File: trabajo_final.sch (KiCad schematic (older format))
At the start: 0 parts

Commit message: cambio de pc
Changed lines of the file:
@@
 F8 "SDA" B R 2750 2050 60
 F9 "SCL" B R 2750 2150 60
-F10 "RXD" B R 2750 2350 60
-F11 "TXD" B R 2750 2450 60
+F10 "RXD" I R 2750 2350 60
+F11 "TXD" O R 2750 2450 60
 F12 "RD" B R 2750 2650 60
 F13 "TD" B R 2750 2750 60
@@
 F23 "LCD_EN" I R 2750 5500 60
 F24 "GPIO0" B R 2750 5750 60
-F25 "GPIO2" B R 2750 5950 60
-F26 "GPIO4" B R 2750 6150 60
-F27 "GPIO6" B R 2750 6350 60
+F25 "GPIO2" I R 2750 5950 60
+F26 "GPIO4" O R 2750 6150 60
+F27 "GPIO6" O R 2750 6350 60
 F28 "RXD1" B R 2750 4250 60
 F29 "TXEN" B R 2750 4050 60
@@
 F40 "LCD2" B R 2750 5200 60
 F41 "LCD1" B R 2750 5100 60
-F42 "GPIO1" B R 2750 5850 60
-F43 "GPIO3" B R 2750 6050 60
-F44 "GPIO5" B R 2750 6250 60
+F42 "GPIO1" O R 2750 5850 60
+F43 "GPIO3" O R 2750 6050 60
+F44 "GPIO5" O R 2750 6250 60
 F45 "GPIO7" B R 2750 6450 60
 F46 "GPIO8" B R 2750 6550 60
@@
 Text Notes 3800 2000 0    60   Italic 12
 I2C
-Text Notes 3750 2300 0    60   Italic 12
+Text Notes 3700 2300 0    60   Italic 12
 RS-232
-Text Notes 3300 5700 0    60   Italic 12
+Text Notes 3300 5800 0    60   Italic 12
 E/S PROPÓSITOS GENERALES
 Wire Wire Line
@@
 F2 "SDA" B L 5250 2050 60
 F3 "SCL" I L 5250 2150 60
-F4 "GPIO6" B L 5250 6350 60
+F4 "GPIO6" I L 5250 6350 60
 F5 "RS232_RXD" O L 5250 2350 60
 F6 "RS232_TXD" I L 5250 2450 60

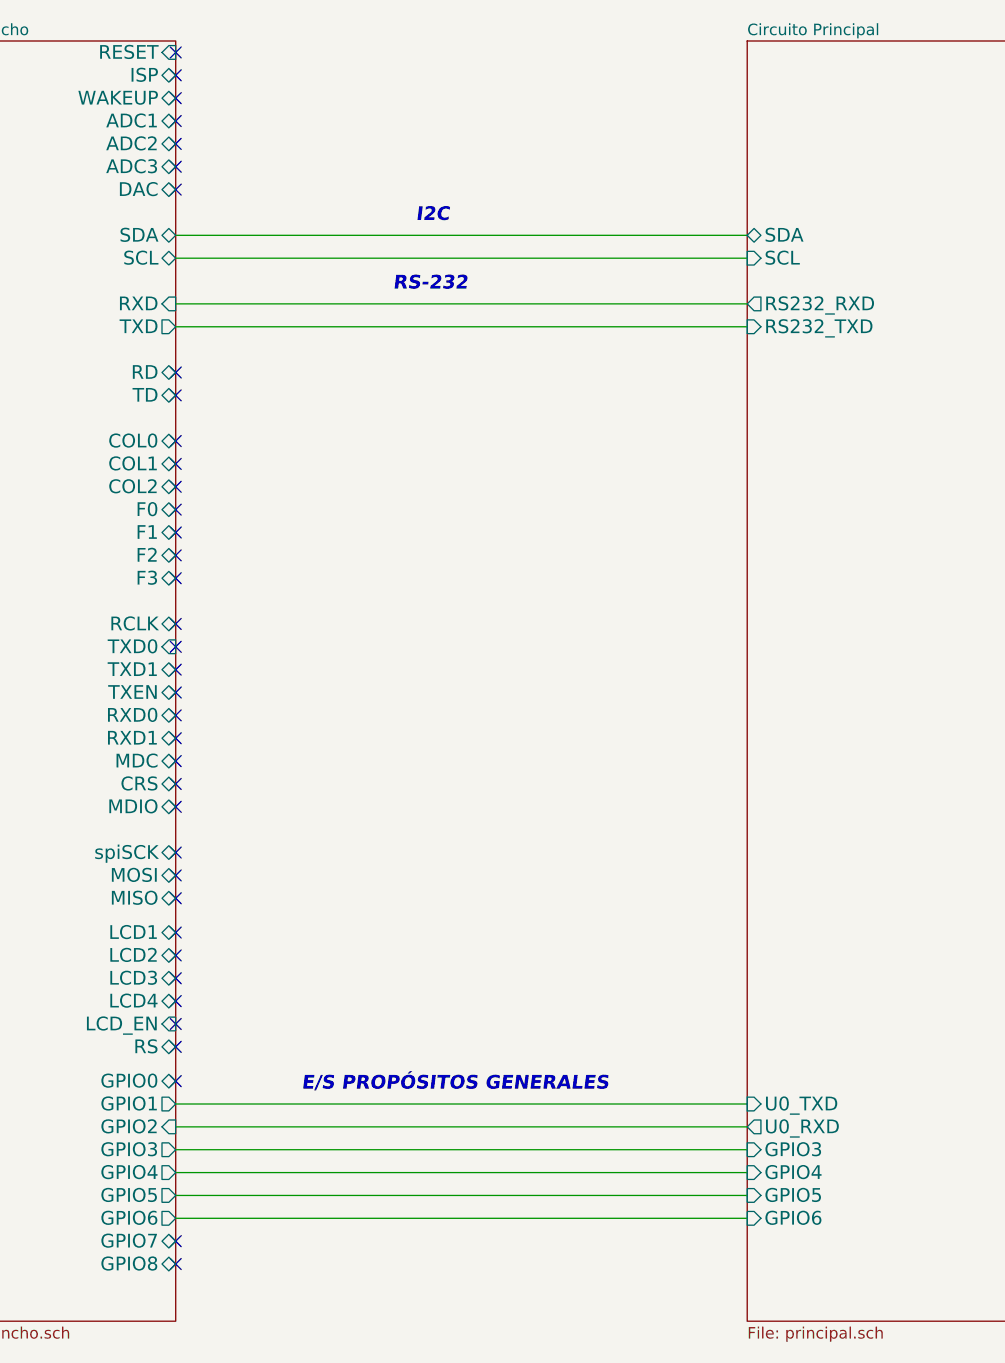
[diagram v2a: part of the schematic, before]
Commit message: agregado buzzer y medidor de batería
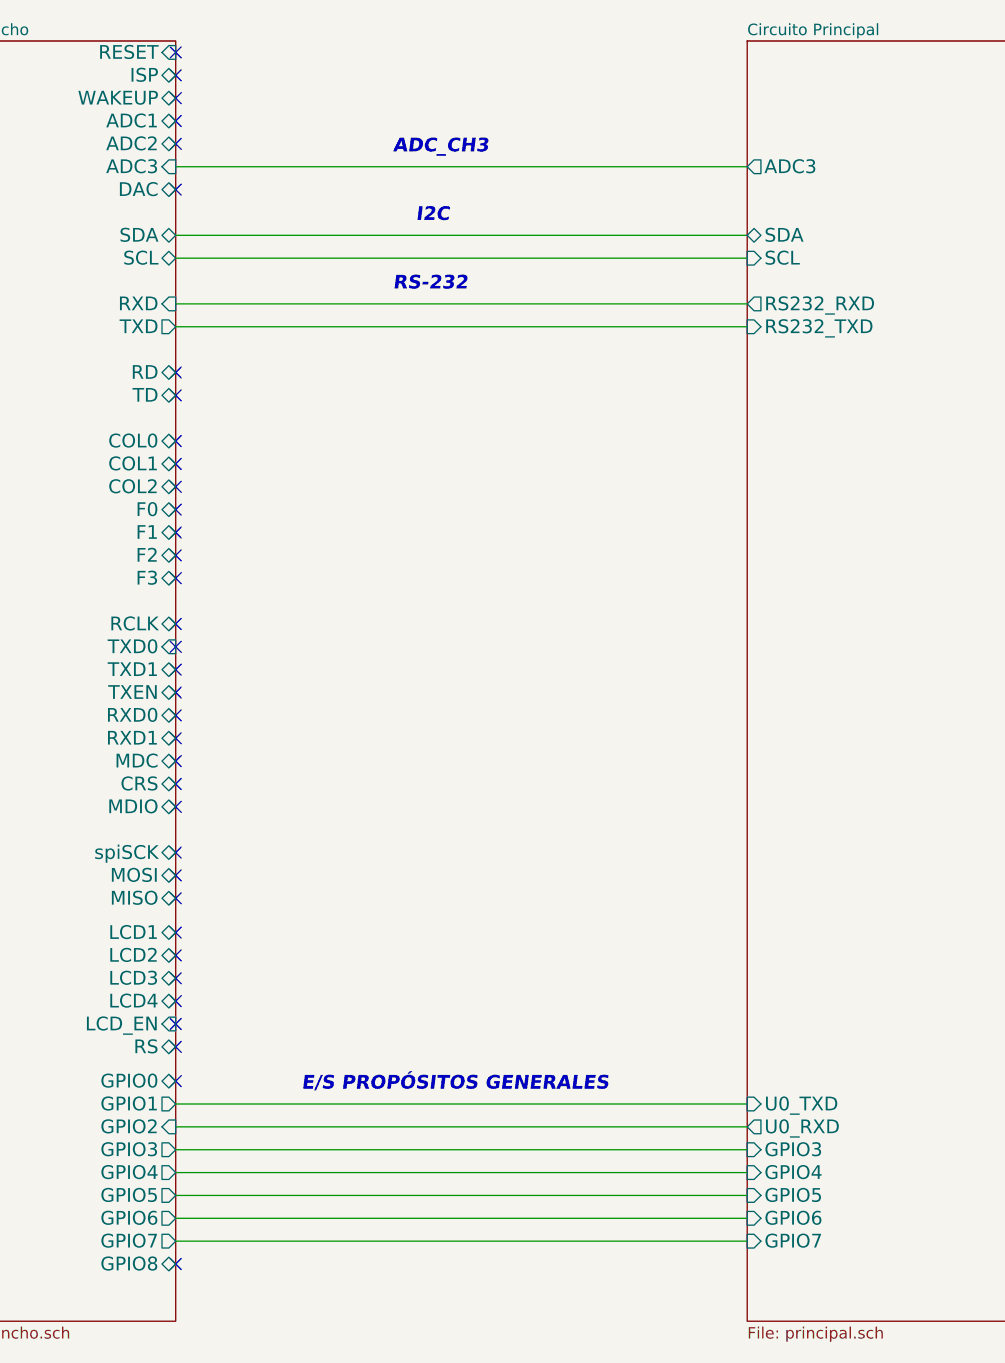
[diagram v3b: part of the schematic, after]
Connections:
- no-connect marks 37 -> 35
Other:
- note added: "ADC_CH3"
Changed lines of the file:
@@
 LIBS:falling_detector-cache
 LIBS:poncho_grande-cache
+LIBS:74xgxx
+LIBS:74xx
+LIBS:ac-dc
+LIBS:actel
+LIBS:adc-dac
+LIBS:Altera
+LIBS:analog_devices
+LIBS:analog_switches
+LIBS:atmel
+LIBS:audio
+LIBS:brooktre
+LIBS:cmos_ieee
+LIBS:cmos4000
+LIBS:conn
+LIBS:contrib
+LIBS:cypress
+LIBS:dc-dc
+LIBS:device
+LIBS:digital-audio
+LIBS:diode
+LIBS:display
+LIBS:dsp
+LIBS:elec-unifil
+LIBS:ESD_Protection
+LIBS:ftdi
+LIBS:gennum
+LIBS:graphic
+LIBS:hc11
+LIBS:intel
+LIBS:interface
+LIBS:ir
+LIBS:Lattice
+LIBS:linear
+LIBS:logo
+LIBS:maxim
+LIBS:memory
+LIBS:microchip
+LIBS:microchip_dspic33dsc
+LIBS:microchip_pic10mcu
+LIBS:microchip_pic12mcu
+LIBS:microchip_pic16mcu
+LIBS:microchip_pic18mcu
+LIBS:microchip_pic32mcu
+LIBS:microcontrollers
+LIBS:motor_drivers
+LIBS:motorola
+LIBS:msp430
+LIBS:nordicsemi
+LIBS:nxp_armmcu
+LIBS:onsemi
+LIBS:opto
+LIBS:Oscillators
+LIBS:philips
+LIBS:power
+LIBS:Power_Management
+LIBS:powerint
+LIBS:pspice
+LIBS:references
+LIBS:regul
+LIBS:relays
+LIBS:rfcom
+LIBS:sensors
+LIBS:silabs
+LIBS:siliconi
+LIBS:stm8
+LIBS:stm32
+LIBS:supertex
+LIBS:switches
+LIBS:texas
+LIBS:transf
+LIBS:transistors
+LIBS:ttl_ieee
+LIBS:valves
+LIBS:video
+LIBS:Xicor
+LIBS:xilinx
+LIBS:Zilog
+LIBS:buzzer
 LIBS:trabajo_final-cache
 EELAYER 25 0
@@
 F2 "RESET" I R 2750 1250 60
 F3 "ISP" B R 2750 1350 60
-F4 "ADC3" B R 2750 1750 60
+F4 "ADC3" I R 2750 1750 60
 F5 "ADC2" B R 2750 1650 60
 F6 "ADC1" B R 2750 1550 60
@@
 F43 "GPIO3" O R 2750 6050 60
 F44 "GPIO5" O R 2750 6250 60
-F45 "GPIO7" B R 2750 6450 60
+F45 "GPIO7" O R 2750 6450 60
 F46 "GPIO8" B R 2750 6550 60
 F47 "COL2" B R 2750 3150 60
@@
 Text Notes 3300 5800 0    60   Italic 12
 E/S PROPÓSITOS GENERALES
-Wire Wire Line
-	5250 6350 2750 6350
-Wire Wire Line
-	2750 6250 5250 6250
-Wire Wire Line
-	5250 6150 2750 6150
-Wire Wire Line
-	2750 6050 5250 6050
-Wire Wire Line
-	5250 5950 2750 5950
-Wire Wire Line
-	5250 5850 2750 5850
-Wire Wire Line
-	5250 2450 2750 2450
-Wire Wire Line
-	2750 2350 5250 2350
-Wire Wire Line
-	2750 2150 5250 2150
-Wire Wire Line
-	5250 2050 2750 2050
 $Comp
 L Logo_Poncho #G1
@@
 F10 "U0_TXD" I L 5250 5850 60
 F11 "U0_RXD" O L 5250 5950 60
+F12 "ADC3" O L 5250 1750 60
+F13 "GPIO7" I L 5250 6450 60
 $EndSheet
 NoConn ~ 2750 1250
@@
 NoConn ~ 2750 1550
 NoConn ~ 2750 1650
-NoConn ~ 2750 1750
 NoConn ~ 2750 1850
 NoConn ~ 2750 2650
@@
 NoConn ~ 2750 5750
 NoConn ~ 2750 6550
-NoConn ~ 2750 6450
+Text Notes 3700 1700 0    60   Italic 12
+ADC_CH3
+Wire Wire Line
+	5250 6450 2750 6450
+Wire Wire Line
+	5250 1750 2750 1750
+Wire Wire Line
+	5250 2050 2750 2050
+Wire Wire Line
+	2750 2150 5250 2150
+Wire Wire Line
+	2750 2350 5250 2350
+Wire Wire Line
+	5250 2450 2750 2450
+Wire Wire Line
+	5250 5850 2750 5850
+Wire Wire Line
+	5250 5950 2750 5950
+Wire Wire Line
+	2750 6050 5250 6050
+Wire Wire Line
+	5250 6150 2750 6150
+Wire Wire Line
+	2750 6250 5250 6250
+Wire Wire Line
+	5250 6350 2750 6350
 $EndSCHEMATC

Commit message: ruteo casi terminado
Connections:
- no-connect marks 35 -> 36
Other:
- note added: "UART0"
- note added: "UART3"
- note removed: "RS-232"
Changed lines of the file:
@@
 encoding utf-8
 Sheet 1 3
-Title "Poncho"
-Date "2016-05-17"
-Rev "1.0"
-Comp "GMotion"
-Comment1 "Autor: Matías Dell'Oso"
-Comment2 ""
+Title "Connections"
+Date "2016-07-23"
+Rev "2.0"
+Comp "Proyecto CIAA - COMPUTADORA INDUSTRIAL ABIERTA ARGENTINA"
+Comment1 "https://github.com/mdelloso/falling_detector"
+Comment2 "Autores y Licencia del template (Matías Dell'Oso - UNLP)"
 Comment3 ""
 Comment4 ""
@@
 F22 "MOSI" B R 2750 4850 60
 F23 "LCD_EN" I R 2750 5500 60
-F24 "GPIO0" B R 2750 5750 60
+F24 "GPIO0" B R 2750 6150 60
 F25 "GPIO2" I R 2750 5950 60
-F26 "GPIO4" O R 2750 6150 60
-F27 "GPIO6" O R 2750 6350 60
+F26 "GPIO4" O R 2750 6350 60
+F27 "GPIO6" O R 2750 6550 60
 F28 "RXD1" B R 2750 4250 60
 F29 "TXEN" B R 2750 4050 60
@@
 F41 "LCD1" B R 2750 5100 60
 F42 "GPIO1" O R 2750 5850 60
-F43 "GPIO3" O R 2750 6050 60
-F44 "GPIO5" O R 2750 6250 60
-F45 "GPIO7" O R 2750 6450 60
-F46 "GPIO8" B R 2750 6550 60
+F43 "GPIO3" O R 2750 6250 60
+F44 "GPIO5" O R 2750 6450 60
+F45 "GPIO7" O R 2750 6650 60
+F46 "GPIO8" B R 2750 6750 60
 F47 "COL2" B R 2750 3150 60
 F48 "WAKEUP" B R 2750 1450 60
 $EndSheet
-Text Notes 3800 2000 0    60   Italic 12
+Text Notes 3900 2000 0    60   Italic 12
 I2C
-Text Notes 3700 2300 0    60   Italic 12
-RS-232
-Text Notes 3300 5800 0    60   Italic 12
+Text Notes 3850 2300 0    60   Italic 12
+UART3
+Text Notes 3300 6200 0    60   Italic 12
 E/S PROPÓSITOS GENERALES
 $Comp
@@
 F2 "SDA" B L 5250 2050 60
 F3 "SCL" I L 5250 2150 60
-F4 "GPIO6" I L 5250 6350 60
+F4 "GPIO6" I L 5250 6550 60
 F5 "RS232_RXD" O L 5250 2350 60
 F6 "RS232_TXD" I L 5250 2450 60
-F7 "GPIO3" I L 5250 6050 60
-F8 "GPIO4" I L 5250 6150 60
-F9 "GPIO5" I L 5250 6250 60
+F7 "GPIO3" I L 5250 6250 60
+F8 "GPIO4" I L 5250 6350 60
+F9 "GPIO5" I L 5250 6450 60
 F10 "U0_TXD" I L 5250 5850 60
 F11 "U0_RXD" O L 5250 5950 60
 F12 "ADC3" O L 5250 1750 60
-F13 "GPIO7" I L 5250 6450 60
+F13 "GPIO7" I L 5250 6650 60
 $EndSheet
 NoConn ~ 2750 1250
@@
 NoConn ~ 2750 5600
 NoConn ~ 2750 5750
-NoConn ~ 2750 6550
-Text Notes 3700 1700 0    60   Italic 12
+NoConn ~ 2750 6750
+Text Notes 3800 1700 0    60   Italic 12
 ADC_CH3
 Wire Wire Line
@@
 	5250 5950 2750 5950
 Wire Wire Line
-	2750 6050 5250 6050
-Wire Wire Line
-	5250 6150 2750 6150
-Wire Wire Line
 	2750 6250 5250 6250
 Wire Wire Line
 	5250 6350 2750 6350
+Wire Wire Line
+	5250 6650 2750 6650
+Wire Wire Line
+	5250 6550 2750 6550
+NoConn ~ 2750 6150
+Text Notes 3800 5800 0    60   Italic 12
+UART0
 $EndSCHEMATC

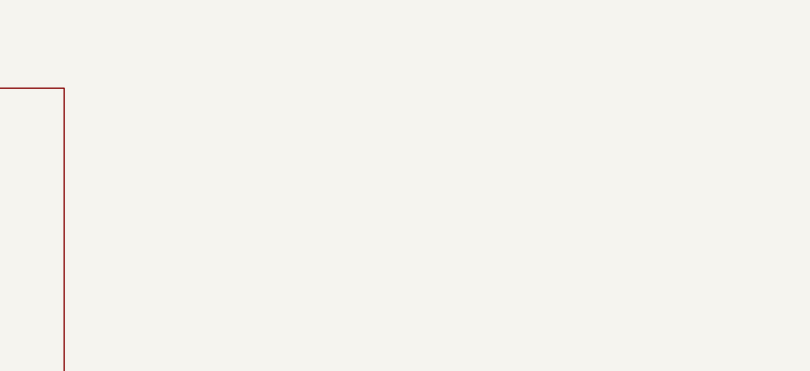
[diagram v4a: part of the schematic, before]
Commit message: Realizando las correcciones correspondientes a la Revision 1
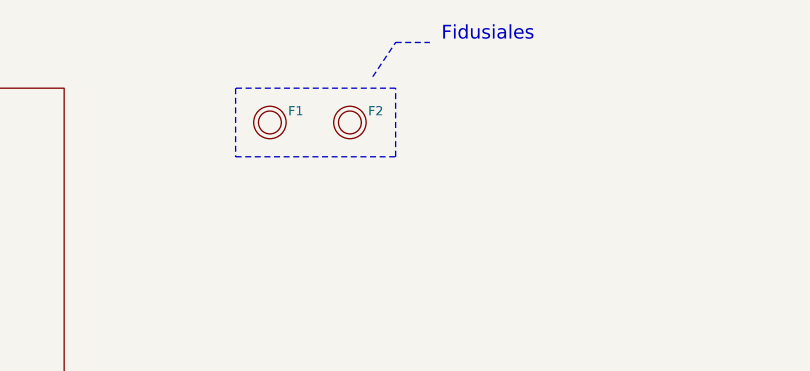
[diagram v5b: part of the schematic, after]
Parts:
- added F1, F2: FIDUCIAL, footprints:Fiducial_1mm, symbol FIDUCIAL
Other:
- note added: "Fidusiales"
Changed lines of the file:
@@
 LIBS:falling_detector-cache
 LIBS:poncho_grande-cache
-LIBS:74xgxx
-LIBS:74xx
-LIBS:ac-dc
-LIBS:actel
-LIBS:adc-dac
-LIBS:Altera
-LIBS:analog_devices
-LIBS:analog_switches
-LIBS:atmel
-LIBS:audio
-LIBS:brooktre
-LIBS:cmos_ieee
-LIBS:cmos4000
-LIBS:conn
-LIBS:contrib
-LIBS:cypress
-LIBS:dc-dc
-LIBS:device
-LIBS:digital-audio
-LIBS:diode
-LIBS:display
-LIBS:dsp
-LIBS:elec-unifil
-LIBS:ESD_Protection
-LIBS:ftdi
-LIBS:gennum
-LIBS:graphic
-LIBS:hc11
-LIBS:intel
-LIBS:interface
-LIBS:ir
-LIBS:Lattice
-LIBS:linear
-LIBS:logo
-LIBS:maxim
-LIBS:memory
-LIBS:microchip
-LIBS:microchip_dspic33dsc
-LIBS:microchip_pic10mcu
-LIBS:microchip_pic12mcu
-LIBS:microchip_pic16mcu
-LIBS:microchip_pic18mcu
-LIBS:microchip_pic32mcu
-LIBS:microcontrollers
-LIBS:motor_drivers
-LIBS:motorola
-LIBS:msp430
-LIBS:nordicsemi
-LIBS:nxp_armmcu
-LIBS:onsemi
-LIBS:opto
-LIBS:Oscillators
-LIBS:philips
+LIBS:buzzer
 LIBS:power
-LIBS:Power_Management
-LIBS:powerint
-LIBS:pspice
-LIBS:references
-LIBS:regul
-LIBS:relays
-LIBS:rfcom
-LIBS:sensors
-LIBS:silabs
-LIBS:siliconi
-LIBS:stm8
-LIBS:stm32
-LIBS:supertex
-LIBS:switches
-LIBS:texas
-LIBS:transf
-LIBS:transistors
-LIBS:ttl_ieee
-LIBS:valves
-LIBS:video
-LIBS:Xicor
-LIBS:xilinx
-LIBS:Zilog
-LIBS:buzzer
+LIBS:ej2cese
 LIBS:trabajo_final-cache
 EELAYER 25 0
@@
 Text Notes 3800 5800 0    60   Italic 12
 UART0
+$Comp
+L FIDUCIAL F1
+U 1 1 579982BE
+P 7500 1350
+F 0 "F1" H 7580 1400 40  0000 L CNN
+F 1 "FIDUCIAL" H 7500 1250 30  0001 C CNN
+F 2 "footprints:Fiducial_1mm" H 7500 1400 60  0001 C CNN
+F 3 "" H 7500 1400 60  0001 C CNN
+F 4 "FIDUCIAL" H 7550 1150 60  0001 C CNN "Descripcion"
+	1    7500 1350
+	1    0    0    -1
+$EndComp
+$Comp
+L FIDUCIAL F2
+U 1 1 57999260
+P 7850 1350
+F 0 "F2" H 7930 1400 40  0000 L CNN
+F 1 "FIDUCIAL" H 7850 1250 30  0001 C CNN
+F 2 "footprints:Fiducial_1mm" H 7850 1400 60  0001 C CNN
+F 3 "" H 7850 1400 60  0001 C CNN
+F 4 "FIDUCIAL" H 7900 1150 60  0001 C CNN "Descripcion"
+	1    7850 1350
+	1    0    0    -1
+$EndComp
+Wire Notes Line
+	7350 1200 7350 1500
+Wire Notes Line
+	8050 1500 8050 1200
+Wire Notes Line
+	8050 1200 7350 1200
+Wire Notes Line
+	7350 1500 8050 1500
+Wire Notes Line
+	7950 1150 8050 1000
+Wire Notes Line
+	8050 1000 8200 1000
+Text Notes 8250 1000 0    60   ~ 0
+Fidusiales
 $EndSCHEMATC

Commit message: versión final
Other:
- note added: "Fiduciales"
- note removed: "Fidusiales"
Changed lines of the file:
@@
 Rev "2.0"
 Comp "CESE - Trabajo final de la materia \"Diseño de Circuitos Impresos\""
-Comment1 "https://github.com/mdelloso/falling_detector"
-Comment2 "Autores: Ver 'doc/CAMBIOS.txt'      Licencia: Ver  'doc/LICENCIA.txt'"
+Comment1 "Autores: Ver 'doc/CAMBIOS.txt'      Licencia: Ver  'doc/LICENCIA.txt'"
+Comment2 ""
 Comment3 ""
 Comment4 ""
@@
 	8050 1000 8200 1000
 Text Notes 8250 1000 0    60   ~ 0
-Fidusiales
+Fiduciales
 $EndSCHEMATC
